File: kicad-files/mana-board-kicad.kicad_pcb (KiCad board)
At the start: 2 copper layers, 200 x 125 mm, 63 parts, among them U1 Pico, U2 74AHCT1G125

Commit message: din't stage the correct file
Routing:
- net /Pi D-: track 174.2 -> 177.0 mm
- net /Pi D+: track 174.4 -> 177.2 mm
- net Net-(USB1-CC1): vias 2 -> 0
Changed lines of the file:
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@@
   (segment (start 205.103165 61.287913) (end 205.103165 63.826446) (width 0.25) (layer "B.Cu") (net 39))
   (segment (start 177.255191 45.5) (end 181.45 45.5) (width 0.25) (layer "F.Cu") (net 40))
+  (segment (start 174.5 42.75) (end 176.276126 44.526126) (width 0.25) (layer "F.Cu") (net 40))
   (segment (start 173.75 42) (end 174.5 42.75) (width 0.25) (layer "F.Cu") (net 40))
+  (segment (start 176.276126 44.526126) (end 176.281317 44.526126) (width 0.25) (layer "F.Cu") (net 40))
   (segment (start 173.75 40.43) (end 173.75 42) (width 0.25) (layer "F.Cu") (net 40))
   (segment (start 176.281317 44.526126) (end 177.255191 45.5) (width 0.25) (layer "F.Cu") (net 40))
-  (via (at 174.5 42.75) (size 0.8) (drill 0.4) (layers "F.Cu" "B.Cu") (net 40))
-  (via (at 176.281317 44.526126) (size 0.8) (drill 0.4) (layers "F.Cu" "B.Cu") (net 40))
-  (segment (start 174.5 42.75) (end 176.276126 44.526126) (width 0.25) (layer "B.Cu") (net 40))
-  (segment (start 176.276126 44.526126) (end 176.281317 44.526126) (width 0.25) (layer "B.Cu") (net 40))
-  (segment (start 251.3255 87.82346) (end 242.17396 96.975) (width 0.2) (layer "F.Cu") (net 41))
+  (segment (start 193.2573 38.9245) (end 246.9927 38.9245) (width 0.2) (layer "F.Cu") (net 41))
   (segment (start 219.331396 96.975) (end 218.000001 98.306395) (width 0.2) (layer "F.Cu") (net 41))
+  (segment (start 218.000001 98.306395) (end 218.000001 99.669998) (width 0.2) (layer "F.Cu") (net 41))
   (segment (start 173.75 39) (end 173.25 39.5) (width 0.2) (layer "F.Cu") (net 41))
   (segment (start 172.25 39.25) (end 172.25 40.43) (width 0.2) (layer "F.Cu") (net 41))
-  (segment (start 173.225 43.1568) (end 173.698211 43.630011) (width 0.2) (layer "F.Cu") (net 41))
+  (segment (start 185.1818 47) (end 193.2573 38.9245) (width 0.2) (layer "F.Cu") (net 41))
+  (segment (start 246.9927 38.9245) (end 251.3255 43.2573) (width 0.2) (layer "F.Cu") (net 41))
   (segment (start 172 39) (end 172.25 39.25) (width 0.2) (layer "F.Cu") (net 41))
-  (segment (start 218.000001 98.306395) (end 218.000001 99.669998) (width 0.2) (layer "F.Cu") (net 41))
+  (segment (start 173.25 40.43) (end 173.25 41.292501) (width 0.2) (layer "F.Cu") (net 41))
+  (segment (start 173.225 41.317501) (end 173.225 43.1568) (width 0.2) (layer "F.Cu") (net 41))
+  (segment (start 173.25 41.292501) (end 173.225 41.317501) (width 0.2) (layer "F.Cu") (net 41))
+  (segment (start 251.3255 87.82346) (end 242.17396 96.975) (width 0.2) (layer "F.Cu") (net 41))
+  (segment (start 251.3255 43.2573) (end 251.3255 87.82346) (width 0.2) (layer "F.Cu") (net 41))
+  (segment (start 177.0682 47) (end 185.1818 47) (width 0.2) (layer "F.Cu") (net 41))
   (segment (start 242.17396 96.975) (end 219.331396 96.975) (width 0.2) (layer "F.Cu") (net 41))
-  (segment (start 180.2573 38.9245) (end 246.9927 38.9245) (width 0.2) (layer "F.Cu") (net 41))
-  (segment (start 246.9927 38.9245) (end 251.3255 43.2573) (width 0.2) (layer "F.Cu") (net 41))
-  (segment (start 173.25 41.292501) (end 173.225 41.317501) (width 0.2) (layer "F.Cu") (net 41))
-  (segment (start 173.25 40.43) (end 173.25 41.292501) (width 0.2) (layer "F.Cu") (net 41))
-  (segment (start 175.551789 43.630011) (end 180.2573 38.9245) (width 0.2) (layer "F.Cu") (net 41))
-  (segment (start 173.698211 43.630011) (end 175.551789 43.630011) (width 0.2) (layer "F.Cu") (net 41))
-  (segment (start 173.225 41.317501) (end 173.225 43.1568) (width 0.2) (layer "F.Cu") (net 41))
-  (segment (start 251.3255 43.2573) (end 251.3255 87.82346) (width 0.2) (layer "F.Cu") (net 41))
   (segment (start 173.25 39.5) (end 173.25 40.43) (width 0.2) (layer "F.Cu") (net 41))
+  (segment (start 173.225 43.1568) (end 177.0682 47) (width 0.2) (layer "F.Cu") (net 41))
   (via (at 173.75 39) (size 0.8) (drill 0.4) (layers "F.Cu" "B.Cu") (net 41))
   (via (at 172 39) (size 0.8) (drill 0.4) (layers "F.Cu" "B.Cu") (net 41))
@@
   (segment (start 172 39) (end 172 38.75) (width 0.2) (layer "B.Cu") (net 41))
   (segment (start 171.75 39.73995) (end 171.75 40.43) (width 0.2) (layer "F.Cu") (net 42))
+  (segment (start 176.8318 47.4) (end 185.4182 47.4) (width 0.2) (layer "F.Cu") (net 42))
+  (segment (start 171.3 39.28995) (end 171.75 39.73995) (width 0.2) (layer "F.Cu") (net 42))
+  (segment (start 185.4182 47.4) (end 193.4937 39.3245) (width 0.2) (layer "F.Cu") (net 42))
+  (segment (start 171.3 38.71005) (end 171.3 39.28995) (width 0.2) (layer "F.Cu") (net 42))
+  (segment (start 246.7563 39.3245) (end 250.8755 43.4437) (width 0.2) (layer "F.Cu") (net 42))
+  (segment (start 172.75 40.43) (end 172.75 38.76005) (width 0.2) (layer "F.Cu") (net 42))
+  (segment (start 242.058274 96.525) (end 219.144999 96.525) (width 0.2) (layer "F.Cu") (net 42))
   (segment (start 250.8755 87.707774) (end 242.058274 96.525) (width 0.2) (layer "F.Cu") (net 42))
-  (segment (start 171.3 39.28995) (end 171.75 39.73995) (width 0.2) (layer "F.Cu") (net 42))
-  (segment (start 173.511811 44.080011) (end 175.738189 44.080011) (width 0.2) (layer "F.Cu") (net 42))
+  (segment (start 193.4937 39.3245) (end 246.7563 39.3245) (width 0.2) (layer "F.Cu") (net 42))
+  (segment (start 250.8755 43.4437) (end 250.8755 87.707774) (width 0.2) (layer "F.Cu") (net 42))
+  (segment (start 172.28995 38.3) (end 171.71005 38.3) (width 0.2) (layer "F.Cu") (net 42))
+  (segment (start 172.75 40.43) (end 172.75 41.292501) (width 0.2) (layer "F.Cu") (net 42))
+  (segment (start 172.75 41.292501) (end 172.775 41.317501) (width 0.2) (layer "F.Cu") (net 42))
+  (segment (start 172.75 38.76005) (end 172.28995 38.3) (width 0.2) (layer "F.Cu") (net 42))
   (segment (start 172.775 41.317501) (end 172.775 43.3432) (width 0.2) (layer "F.Cu") (net 42))
-  (segment (start 171.3 38.71005) (end 171.3 39.28995) (width 0.2) (layer "F.Cu") (net 42))
-  (segment (start 172.75 40.43) (end 172.75 38.76005) (width 0.2) (layer "F.Cu") (net 42))
-  (segment (start 172.75 41.292501) (end 172.775 41.317501) (width 0.2) (layer "F.Cu") (net 42))
-  (segment (start 175.738189 44.080011) (end 180.4437 39.3745) (width 0.2) (layer "F.Cu") (net 42))
-  (segment (start 246.8063 39.3745) (end 250.8755 43.4437) (width 0.2) (layer "F.Cu") (net 42))
-  (segment (start 180.4437 39.3745) (end 246.8063 39.3745) (width 0.2) (layer "F.Cu") (net 42))
-  (segment (start 172.775 43.3432) (end 173.511811 44.080011) (width 0.2) (layer "F.Cu") (net 42))
+  (segment (start 171.71005 38.3) (end 171.3 38.71005) (width 0.2) (layer "F.Cu") (net 42))
   (segment (start 219.144999 96.525) (end 216 99.669999) (width 0.2) (layer "F.Cu") (net 42))
-  (segment (start 172.28995 38.3) (end 171.71005 38.3) (width 0.2) (layer "F.Cu") (net 42))
-  (segment (start 250.8755 43.4437) (end 250.8755 87.707774) (width 0.2) (layer "F.Cu") (net 42))
-  (segment (start 172.75 38.76005) (end 172.28995 38.3) (width 0.2) (layer "F.Cu") (net 42))
-  (segment (start 172.75 40.43) (end 172.75 41.292501) (width 0.2) (layer "F.Cu") (net 42))
-  (segment (start 171.71005 38.3) (end 171.3 38.71005) (width 0.2) (layer "F.Cu") (net 42))
-  (segment (start 242.058274 96.525) (end 219.144999 96.525) (width 0.2) (layer "F.Cu") (net 42))
+  (segment (start 172.775 43.3432) (end 176.8318 47.4) (width 0.2) (layer "F.Cu") (net 42))
   (segment (start 170.75 40.43) (end 170.75 46.25) (width 0.25) (layer "F.Cu") (net 45))
   (segment (start 173.5 49) (end 181.45 49) (width 0.25) (layer "F.Cu") (net 45))

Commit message: Change mounting holes to M3, separate LED Data line
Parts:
- REF** (x6): value MountingHole_2.1mm -> MountingHole_3mm; footprint ManaBoard:MountingHole_2.1mm -> MountingHole:MountingHole_3mm
- moved C1 9.57 mm to (245.5, 115.5), turned to 90 degrees
- moved R6 2.12 mm to (244.0, 122.2), turned to 0 degrees
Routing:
- net Net-(U1-GPIO4): track 295.8 -> 224.6 mm
- net Net-(U1-GPIO3): track 265.1 -> 193.9 mm
- net Net-(U1-GPIO5): track 244.6 -> 173.4 mm
- net 5V: track 940.3 -> 931.6 mm
- net Net-(U1-GPIO21): track 261.7 -> 268.2 mm
- net Net-(U1-GPIO20): track 241.0 -> 247.5 mm
- net Net-(U1-GPIO19): track 79.1 -> 85.6 mm
- net Net-(U1-GPIO18): track 97.7 -> 104.2 mm
- net Net-(U1-GPIO17): track 353.4 -> 359.9 mm
- net Net-(U1-GPIO16): track 337.1 -> 343.6 mm
- net Net-(U1-RUN): track 22.5 -> 28.5 mm
- net Net-(U1-GPIO2): track 119.2 -> 113.6 mm, vias 0 -> 1
- net RGBDATA_5V: track 269.4 -> 274.0 mm
- net Net-(D1-DOUT): track 181.7 -> 179.6 mm
- net Net-(U2-Y): track 4.11 -> 3.49 mm
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
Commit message: Cleaned up routing, cleanup todo
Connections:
- D13 pad 2: unconnected-(D13-DOUT-Pad2) -> Net-(D13-DOUT)
- D13 pad 4: Net-(D1-DOUT) -> Net-(D13-DIN)
- D2 pad 2: Net-(D2-DOUT) -> unconnected-(D2-DOUT-Pad2)
- D2 pad 4: Net-(D1-DOUT) -> Net-(D13-DIN)
- D3 pad 4: Net-(D2-DOUT) -> Net-(D1-DOUT)
- D4 pad 2: Net-(D4-DOUT) -> Net-(D13-DIN)
- D5 pad 4: Net-(D4-DOUT) -> Net-(D13-DOUT)
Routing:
- net Net-(D13-DIN): track 0.00 -> 173.9 mm
- net 5V: track 931.6 -> 769.0 mm
- net Net-(D1-DOUT): track 179.6 -> 23.2 mm
- net Net-(D2-DOUT): track 102.5 -> 0.00 mm
- net Net-(D13-DOUT): track 0.00 -> 70.3 mm
- net Net-(U1-GPIO20): track 247.5 -> 309.0 mm
- net Net-(U1-GPIO3): track 193.9 -> 135.7 mm
- net Net-(D4-DOUT): track 34.5 -> 0.00 mm
- net Net-(U1-GPIO16): track 343.6 -> 319.0 mm
- net Net-(U1-GPIO21): track 268.2 -> 292.0 mm
- net Net-(U1-GPIO4): track 224.6 -> 203.2 mm
- net Net-(U1-GPIO5): track 173.4 -> 152.4 mm
- net Net-(U1-GPIO10): track 338.6 -> 323.0 mm
- net Net-(U1-GPIO11): track 347.2 -> 332.6 mm
- net Net-(U1-GPIO12): track 369.9 -> 357.3 mm
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
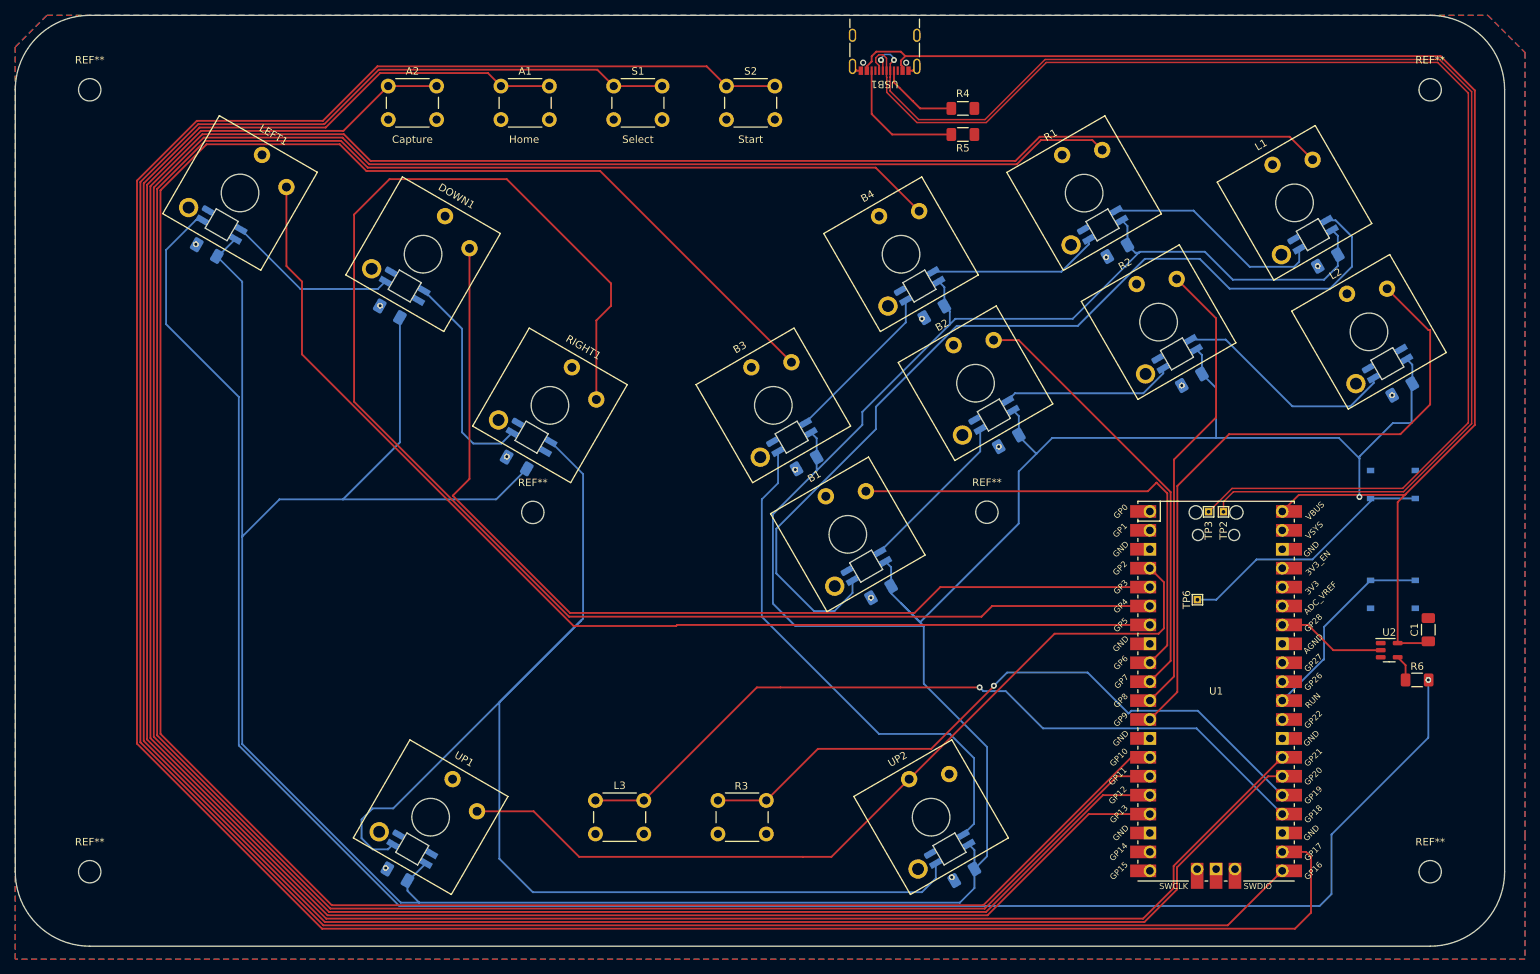
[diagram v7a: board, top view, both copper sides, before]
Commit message: Move parallel UP LEDs to the end of the LED chain
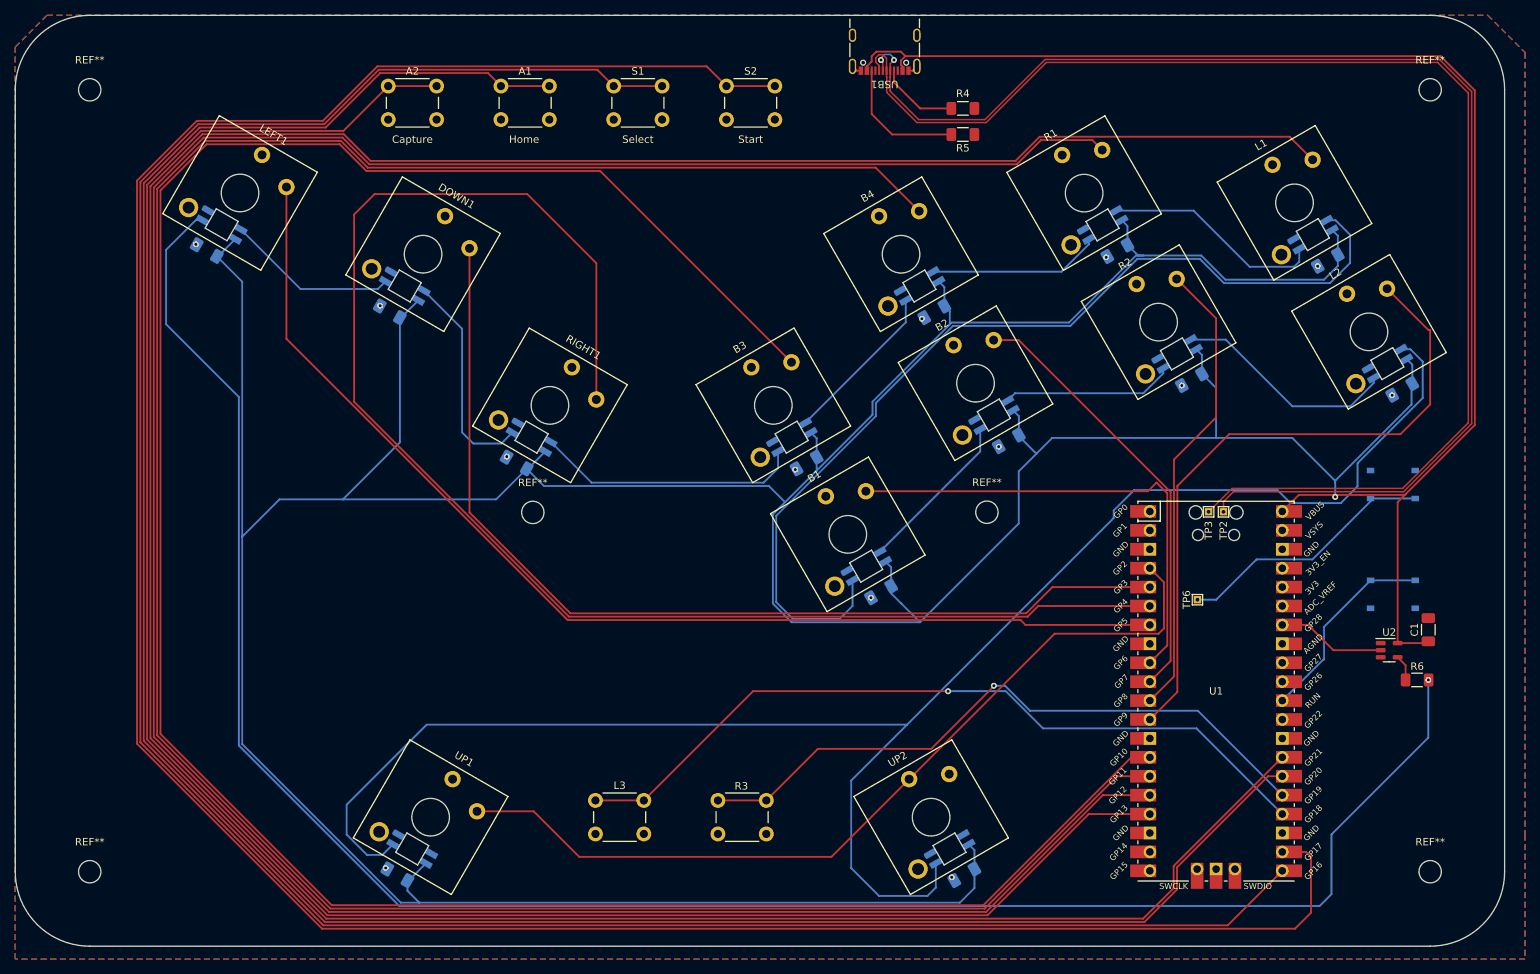
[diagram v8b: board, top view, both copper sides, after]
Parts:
- D12: renamed from D13; value SK6812MINI-E -> SK6812MINI
- D13: renamed from D2; value SK6812MINI -> SK6812MINI-E
- D3: renamed from D4; value SK6812MINI -> SK6812MINI-E
- D4: renamed from D5; value SK6812MINI -> SK6812MINI-E
- renumbered D11 to D10, D12 to D11, D3 to D2, D6 to D5, D7 to D6, D8 to D7, D9 to D8, D10 to D9
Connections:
- D11 pad 2: unconnected-(D12-DOUT-Pad2) -> Net-(D11-DOUT)
- D12 pad 2: Net-(D13-DOUT) -> unconnected-(D12-DOUT-Pad2)
- D12 pad 4: Net-(D13-DIN) -> Net-(D11-DOUT)
- D13 pad 4: Net-(D13-DIN) -> Net-(D11-DOUT)
- D3 pad 2: Net-(D13-DIN) -> Net-(D3-DOUT)
- D4 pad 4: Net-(D13-DOUT) -> Net-(D3-DOUT)
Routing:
- net Net-(D11-DOUT): track 0.00 -> 230.4 mm
- net Net-(D13-DIN): track 173.9 -> 0.00 mm
- net Net-(D13-DOUT): track 70.3 -> 0.00 mm
- net Net-(D3-DOUT): track 0.00 -> 35.8 mm
- net Net-(D7-DOUT): track 126.3 -> 129.5 mm
- net Net-(U1-GPIO4): track 203.2 -> 200.4 mm
- net Net-(U1-GPIO3): track 135.7 -> 133.9 mm
- net Net-(U1-GPIO19): track 90.1 -> 88.3 mm
